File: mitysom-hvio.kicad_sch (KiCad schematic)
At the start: 13 parts, among them J100 Plug_Samtec_SEAM-50-02.0-L-08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, U501 LSF0108RKSR, U502 LSF0108RKSR

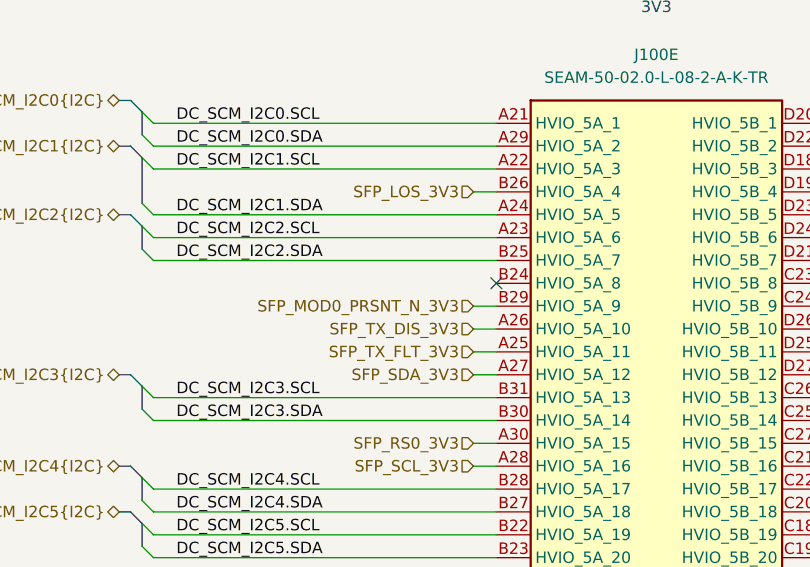
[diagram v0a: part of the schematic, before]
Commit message: [#100501] Connect PECI ALERT to FPGA HVIO pin
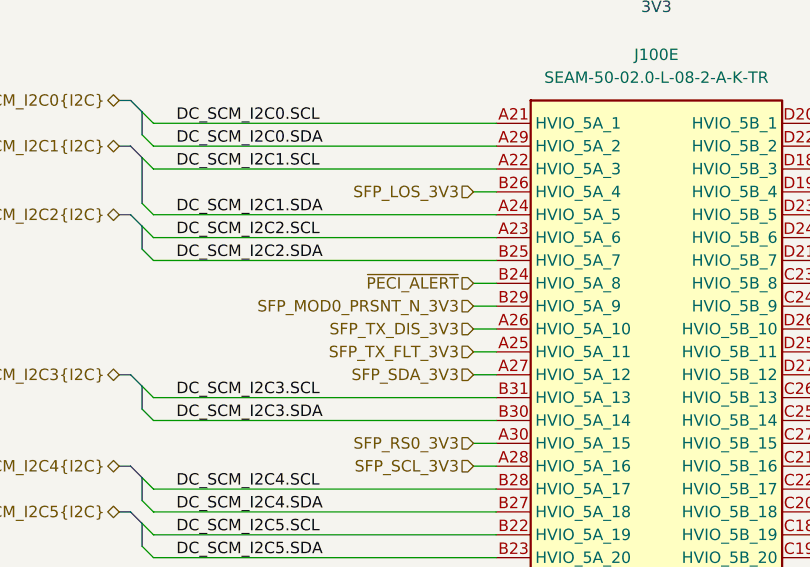
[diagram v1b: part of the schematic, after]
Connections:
- net ~{PECI_ALERT}: now reaches J100.B24 (HVIO_5A_8)
- no-connect marks 11 -> 10
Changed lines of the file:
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@@
 	)
 	(no_connect
-		(at 132.08 231.14)
-	)
-	(no_connect
 		(at 77.47 152.4)
 	)
@@
 	(wire
 		(pts
+			(xy 129.54 231.14) (xy 132.08 231.14)
+		)
+		(stroke
+			(width 0)
+			(type default)
+		)
+	)
+	(wire
+		(pts
 			(xy 374.65 121.92) (xy 372.11 121.92)
 		)
@@
 		(effects
 			(font
+				(size 1.27 1.27)
+			)
+			(justify right)
+		)
+	)
+	(hierarchical_label "~{PECI_ALERT}"
+		(shape input)
+		(at 129.54 231.14 180)
+		(effects
+			(font

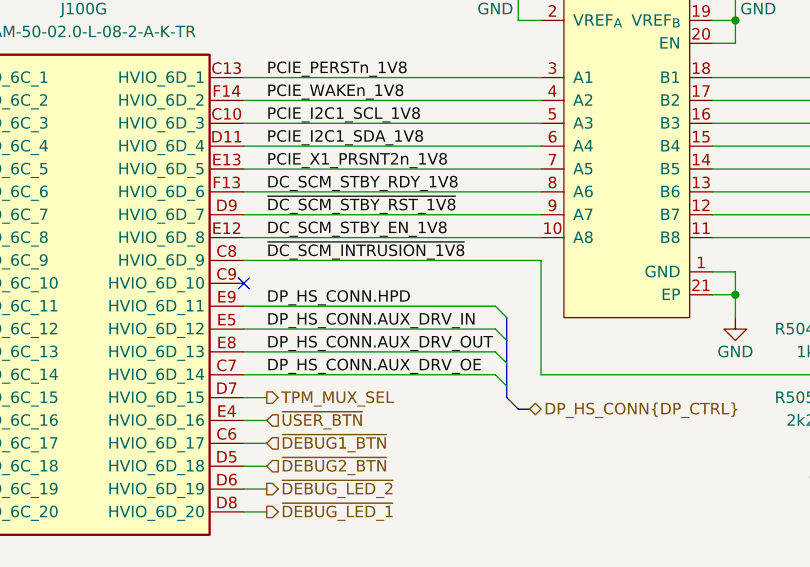
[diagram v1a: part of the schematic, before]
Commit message: [#100501] Change BIOS from BGA to SOIC, add series termination resistors, connect BIOS_RST signal to FPGA
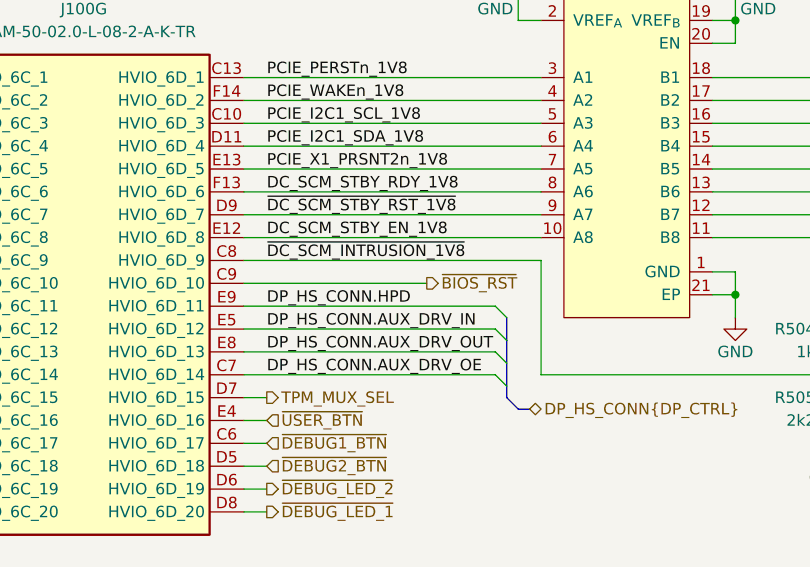
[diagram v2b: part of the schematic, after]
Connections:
- net ~{BIOS_RST}: now reaches J100.C9 (HVIO_6D_10)
- no-connect marks 10 -> 9
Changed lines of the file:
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@@
 	)
 	(no_connect
-		(at 302.26 163.83)
-	)
-	(no_connect
 		(at 96.52 147.32)
 	)
@@
 	(wire
 		(pts
+			(xy 302.26 163.83) (xy 322.58 163.83)
+		)
+		(stroke
+			(width 0)
+			(type default)
+		)
+	)
+	(wire
+		(pts
 			(xy 356.87 121.92) (xy 356.87 134.62)
 		)
@@
 		(effects
 			(font
+				(size 1.27 1.27)
+			)
+			(justify left)
+		)
+	)
+	(hierarchical_label "~{BIOS_RST}"
+		(shape output)
+		(at 322.58 163.83 0)
+		(effects
+			(font

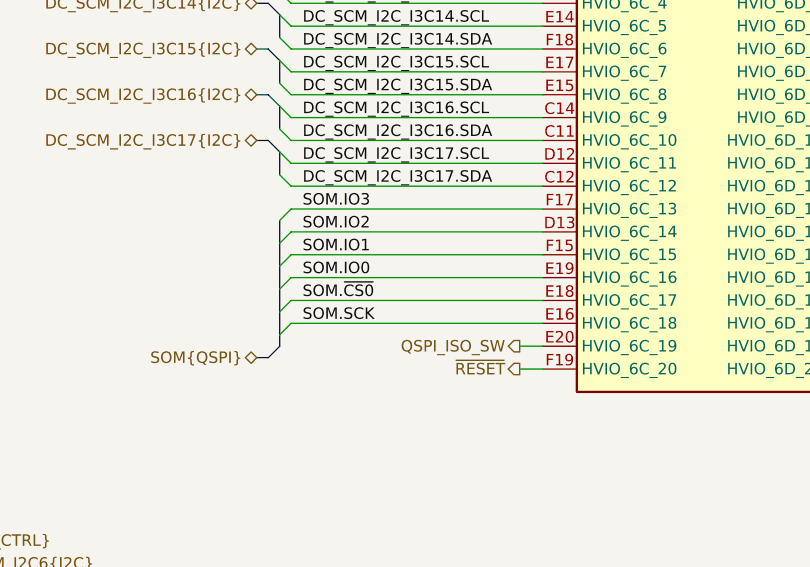
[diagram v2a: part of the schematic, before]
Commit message: [#100501] Add 0Rs to FPGA HVIO QSPI
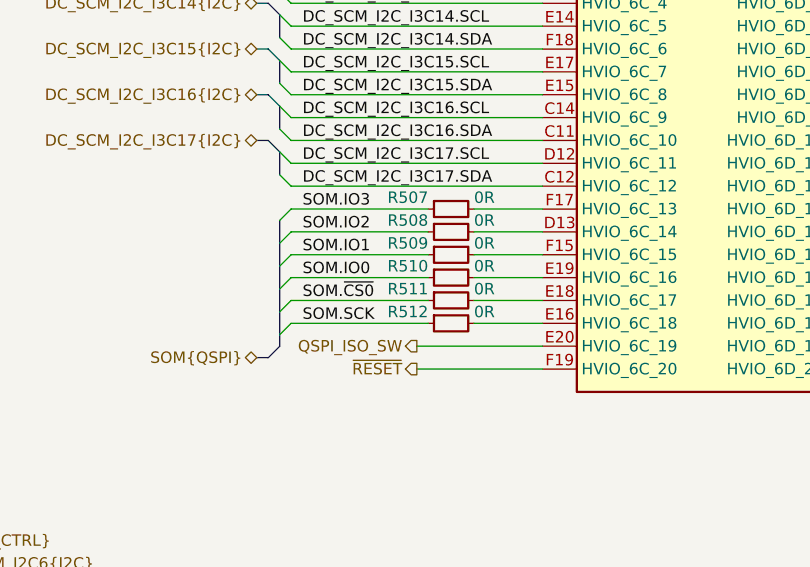
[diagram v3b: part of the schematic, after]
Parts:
- added R507, R508, R509, R510, R511, R512: R_0R_0402, antmicro-footprints:R_0402_1005Metric, symbol antmicroResistors0402:R_0R_0402
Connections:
- net SOM.IO0: now also R510.1; no longer J100.E19 (HVIO_6C_16)
- net SOM.IO1: now also R509.1; no longer J100.F15 (HVIO_6C_15)
- net SOM.IO2: now also R508.1; no longer J100.D13 (HVIO_6C_14)
- net SOM.IO3: now also R507.1; no longer J100.F17 (HVIO_6C_13)
- net SOM.SCK: now also R512.1; no longer J100.E16 (HVIO_6C_18)
- net SOM.~{CS0}: now also R511.1; no longer J100.E18 (HVIO_6C_17)
- new net: J100.D13 (HVIO_6C_14), R508.2
- new net: J100.F15 (HVIO_6C_15), R509.2
- new net: J100.E18 (HVIO_6C_17), R511.2
- new net: J100.E19 (HVIO_6C_16), R510.2
- new net: J100.E16 (HVIO_6C_18), R512.2
- new net: J100.F17 (HVIO_6C_13), R507.2

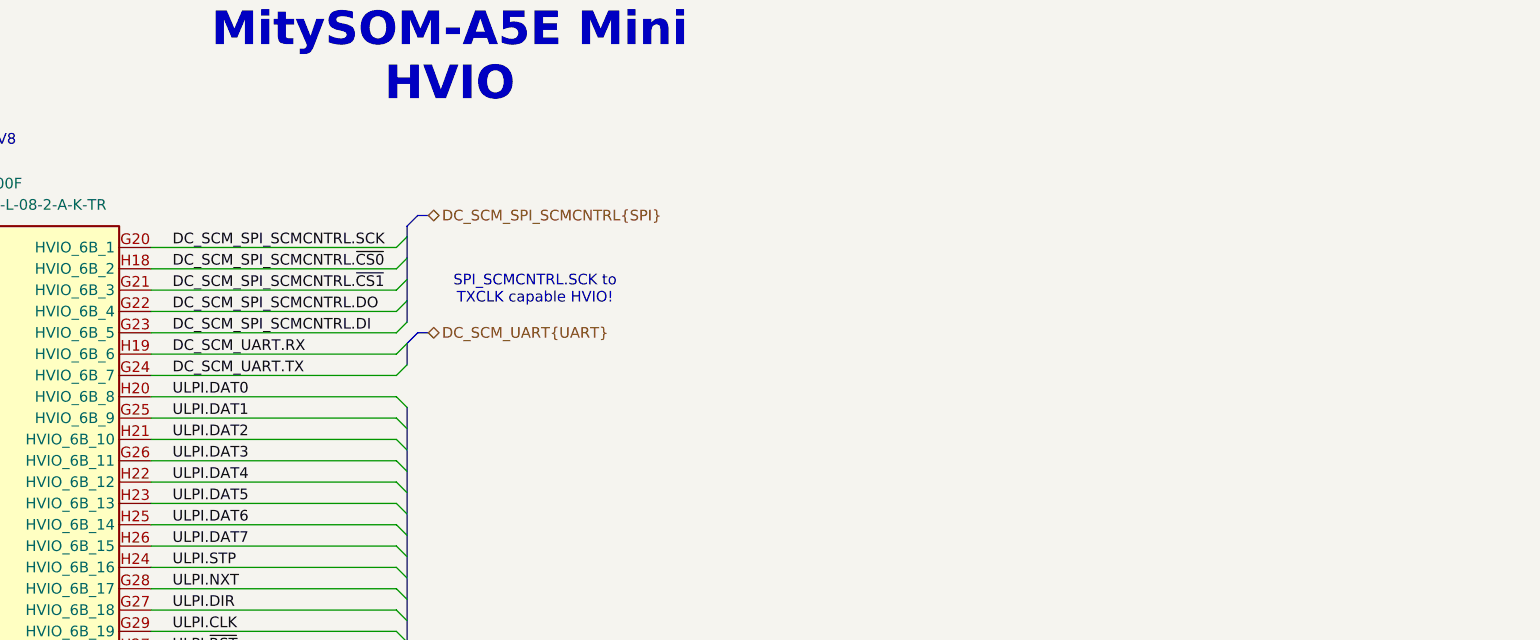
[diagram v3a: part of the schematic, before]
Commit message: [#100501] Move UART level shifter from DC-SCM to HVIO schematic sheet
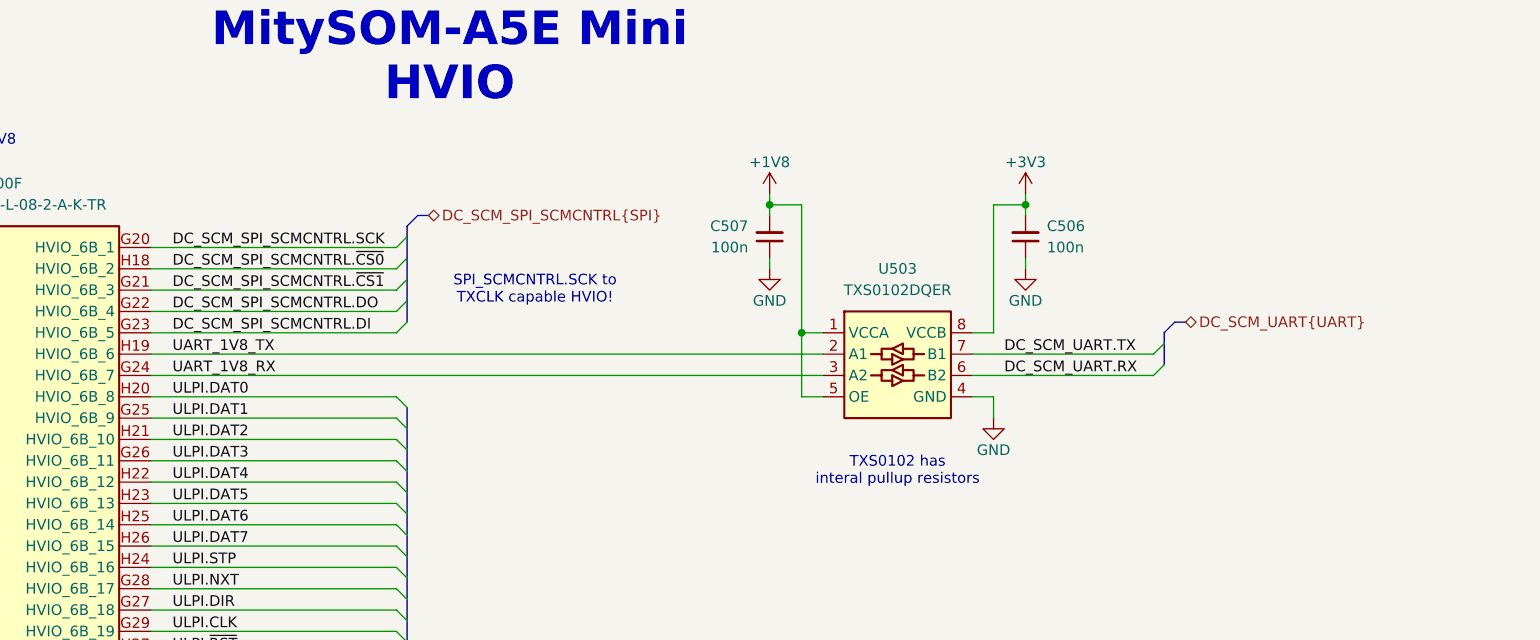
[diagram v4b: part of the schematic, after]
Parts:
- added C506, C507: C_100n_0402, antmicro-footprints:C_0402_1005Metric, symbol antmicroCapacitors0402:C_100n_0402
- added U503: TXS0102DQER, antmicro-footprints:X2SON8_1.4x1x0.32mm_P0.35mm, symbol antmicroLogicTranslatorsLevelShifters:TXS0102DQER
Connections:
- net +1V8: now also C507.2, U503.1 (VCCA), U503.5 (OE)
- net +3V3: now also C506.2, U503.8 (VCCB)
- net DC_SCM_UART.RX: now also U503.6 (B2); no longer J100.H19 (HVIO_6B_6)
- net DC_SCM_UART.TX: now also U503.7 (B1); no longer J100.G24 (HVIO_6B_7)
- net GND: now also C506.1, C507.1, U503.4 (GND)
- new net UART_1V8_RX: J100.G24 (HVIO_6B_7), U503.3 (A2)
- new net UART_1V8_TX: J100.H19 (HVIO_6B_6), U503.2 (A1)
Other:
- note added: "TXS0102 has interal pullup resistors"

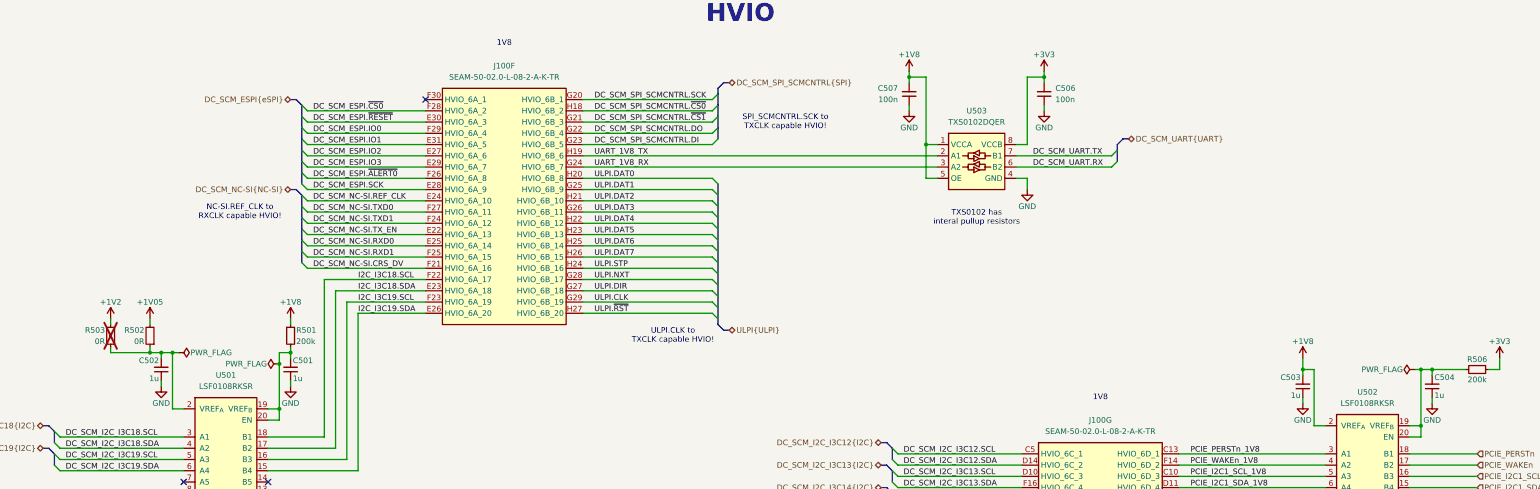
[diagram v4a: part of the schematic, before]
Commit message: [#100501] Reduce LSF0108 decoupling capacitors from 1uF to 100nF
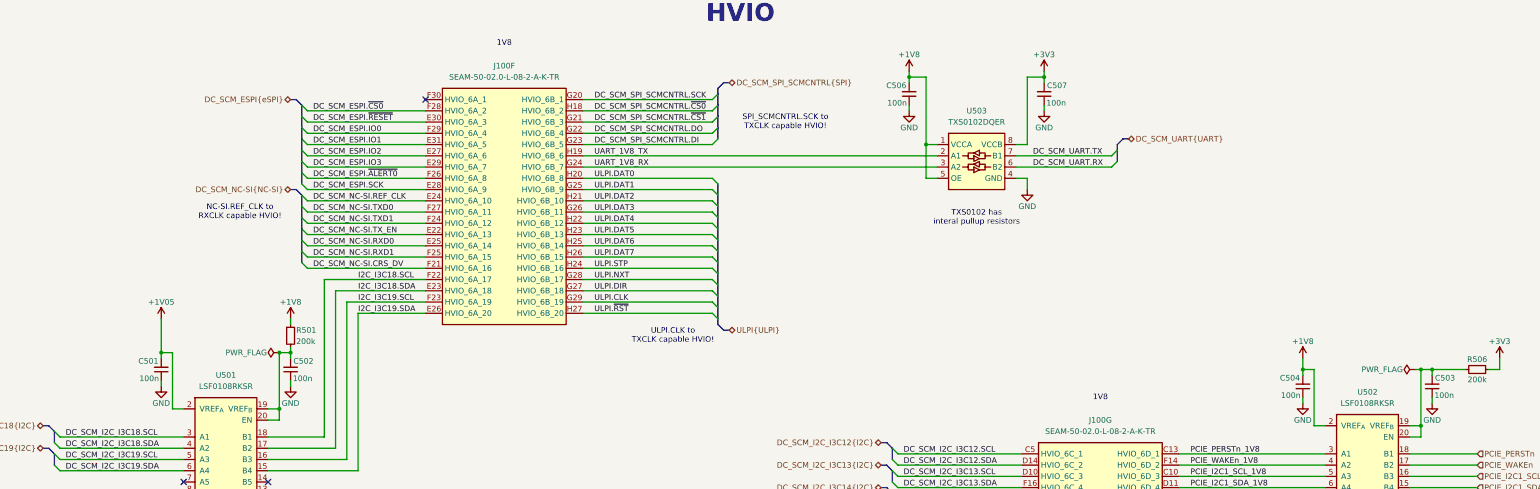
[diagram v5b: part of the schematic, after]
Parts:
- removed C501, C502, C503, C504: C_1u_0402, antmicro-footprints:C_0402_1005Metric, symbol antmicroCapacitors0402:C_1u_0402
- removed R502, R503: R_0R_0402, antmicro-footprints:R_0402_1005Metric, symbol antmicroResistors0402:R_0R_0402
- added C501, C502, C503, C504: C_100n_0402, antmicro-footprints:C_0402_1005Metric, symbol antmicroCapacitors0402:C_100n_0402
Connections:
- net +1V05: now also U501.2 (VREF_{A}), C501.2
- net +1V8: now also C506.2, C504.2; no longer C507.2
- net +3V3: now also C507.2; no longer C506.2
- net GND: now also C501.1, C502.1, C503.1, C504.1
- net at R506.2, U502.19 (VREF_{B}), U502.20 (EN): now also C503.2
- net at R501.2, U501.19 (VREF_{B}), U501.20 (EN): now also C502.2

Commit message: [#100282] Add missing schematic sheet names and align them all
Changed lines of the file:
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@@
 	(text "MitySOM-A5E Mini\nHVIO"
 		(exclude_from_sim no)
-		(at 203.2 38.354 0)
+		(at 210.82 38.1 0)
 		(effects
 			(font

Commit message: [#100501] Reannotate schematic
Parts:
- renumbered C506 to C19, C507 to C20, C501 to C21, C502 to C22, C504 to C23, C503 to C24, J100 to J1, R501 to R10, R506 to R11, R507 to R12, R504 to R13, R508 to R14, R509 to R15, R510 to R16, R505 to R17, R511 to R18, R512 to R19, U503 to U1, U501 to U2, U502 to U3
